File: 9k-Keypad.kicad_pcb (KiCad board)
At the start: 2 copper layers, 66.7 x 4 mm, 36 parts, among them J1 USB_C_Receptacle_USB2.0, U1 ATmega32U4-AU, Y1 16MHz

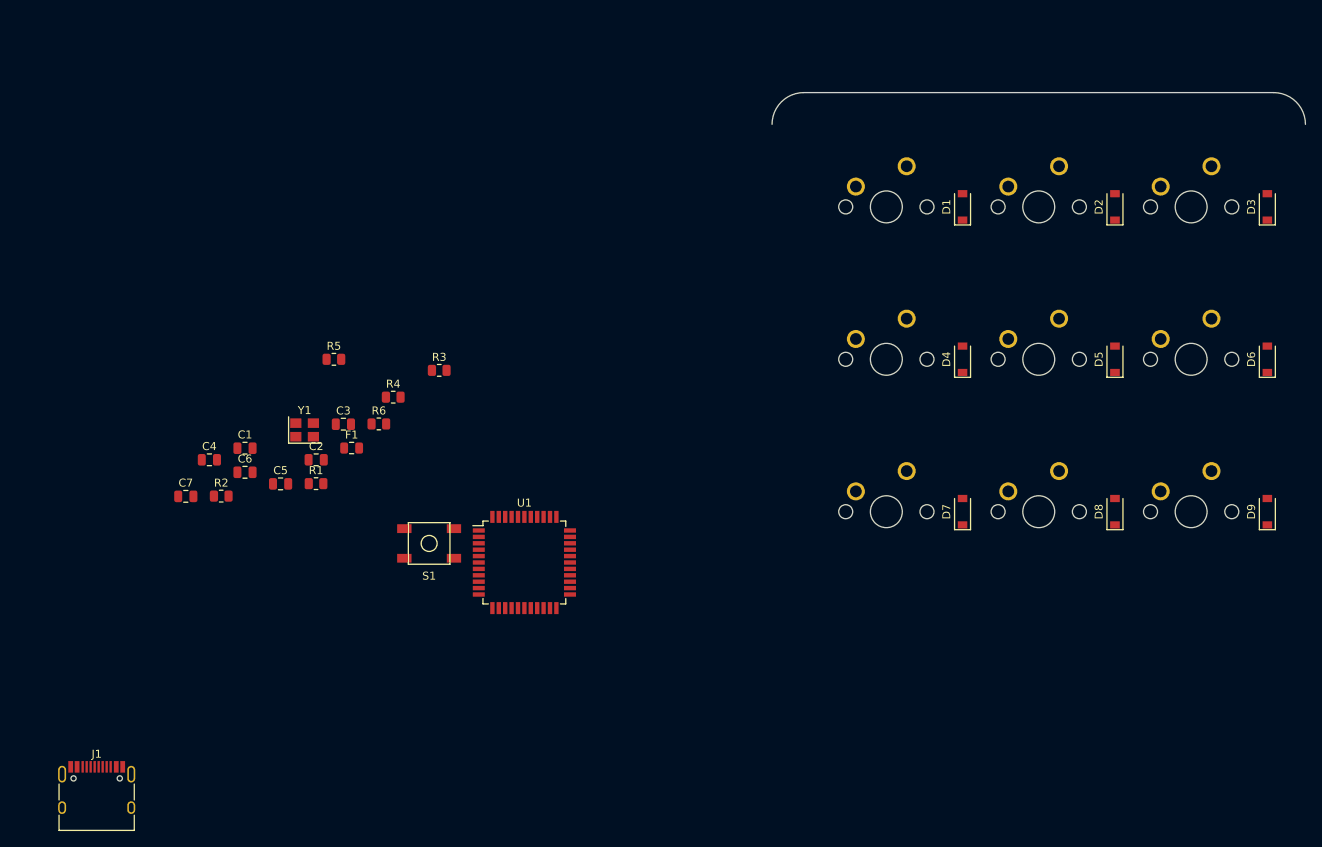
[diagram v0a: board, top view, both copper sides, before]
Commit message: fix various routing issues
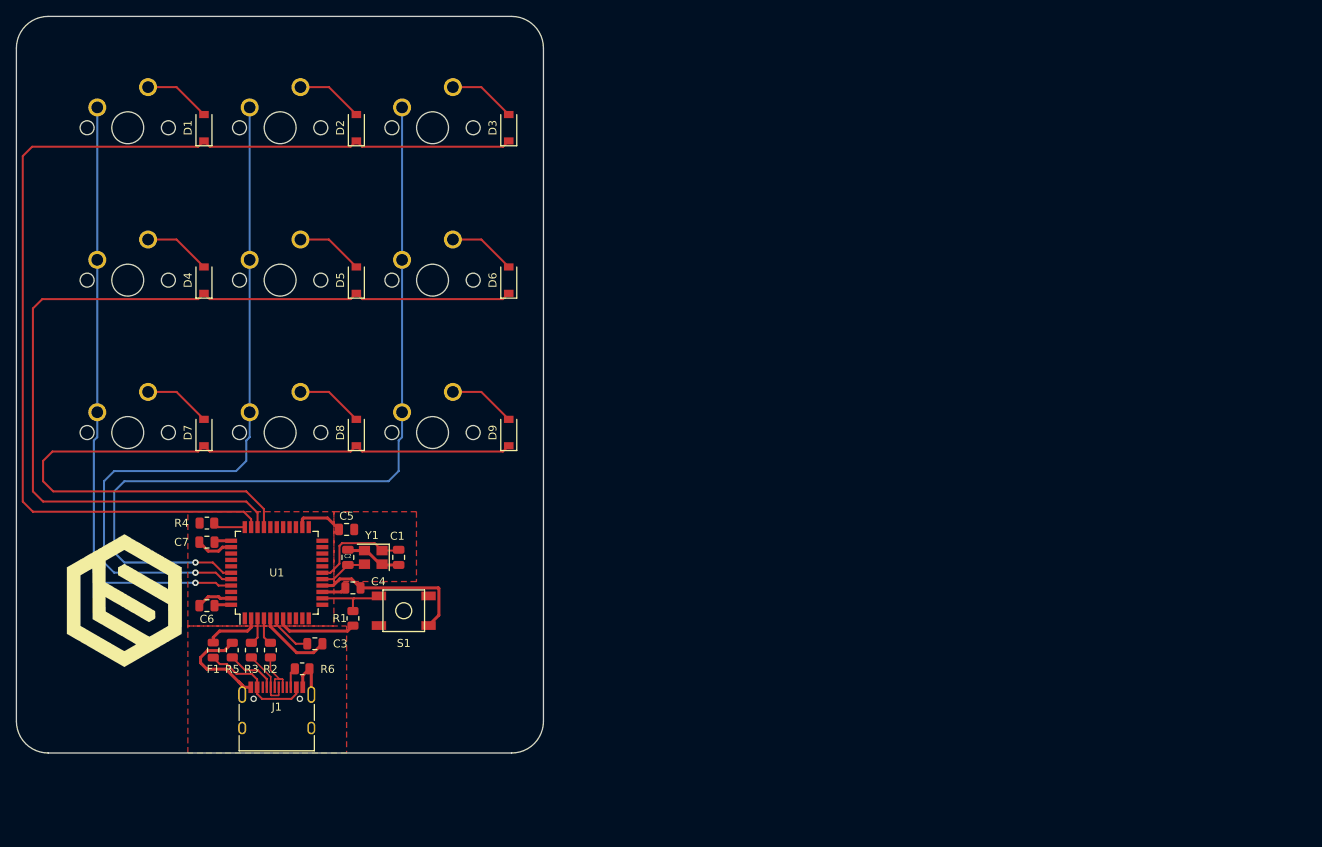
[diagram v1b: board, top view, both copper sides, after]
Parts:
- added G***: LOGO, kiCad 6.0:SL Logo, F.Cu at (95.2, 138.1)
- moved D1 95.3 mm to (105.2, 79.0)
- moved D4 95.3 mm to (105.2, 98.1)
- moved D7 95.3 mm to (105.2, 117.1)
- moved MX1 95.3 mm to (95.7, 79.0)
- moved MX2 95.3 mm to (114.7, 79.0)
- moved MX4 95.3 mm to (95.7, 98.1)
- moved MX5 95.3 mm to (114.7, 98.1)
- moved MX7 95.3 mm to (95.7, 117.1)
- moved MX8 95.3 mm to (114.7, 117.1)
- moved D2 95.3 mm to (124.3, 79.0)
- moved D3 95.3 mm to (143.3, 79.0)
- moved D5 95.3 mm to (124.3, 98.1)
- moved D6 95.3 mm to (143.3, 98.1)
- moved D8 95.3 mm to (124.3, 117.1)
- moved D9 95.3 mm to (143.3, 117.1)
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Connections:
- U1 pad 30: unconnected-(U1-Pad30) -> ROW2
- U1 pad 31: unconnected-(U1-Pad31) -> ROW1
- U1 pad 32: unconnected-(U1-Pad32) -> ROW0
- U1 pad 39: unconnected-(U1-Pad39) -> COL2
- U1 pad 40: unconnected-(U1-Pad40) -> COL1
- U1 pad 41: unconnected-(U1-Pad41) -> COL0
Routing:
- net ROW0: track 0.00 -> 136.4 mm
- net ROW1: track 0.00 -> 115.3 mm
- net COL2: track 0.00 -> 105.5 mm, vias 0 -> 1
- net ROW2: track 0.00 -> 94.0 mm
- net COL1: track 0.00 -> 90.1 mm, vias 0 -> 1
- net COL0: track 0.00 -> 76.2 mm, vias 0 -> 1
- net GND: track 0.00 -> 66.9 mm
- net +5V: track 0.00 -> 30.8 mm
- net VCC: track 0.00 -> 14.7 mm
- net Net-(C1-Pad1): track 0.00 -> 12.8 mm
- net Net-(R1-Pad2): track 0.00 -> 8.84 mm
- net Net-(D3-Pad2): track 0.00 -> 8.41 mm
- net Net-(D9-Pad2): track 0.00 -> 8.41 mm
- net Net-(D6-Pad2): track 0.00 -> 8.41 mm
- net Net-(D2-Pad2): track 0.00 -> 8.41 mm
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- added copper zone on F.Cu, net GND
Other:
- board size 66.7 x 4 mm -> 65.9 x 92.1 mm

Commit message: Finished Design
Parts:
- added REF**: MountingHole_3.5mm, MountingHole:MountingHole_3.5mm, F.Cu at (85.7, 69.1)
- added REF**: MountingHole_3.5mm, MountingHole:MountingHole_3.5mm, F.Cu at (143.7, 151.6)
- added REF**: MountingHole_3.5mm, MountingHole:MountingHole_3.5mm, F.Cu at (143.7, 69.1)
- added REF**: MountingHole_3.5mm, MountingHole:MountingHole_3.5mm, F.Cu at (85.7, 151.6)
- moved C4 8.09 mm to (131.8, 134.9), turned to 90 degrees
- moved C7 3.18 mm to (102.4, 131.0), turned to -90 degrees
- moved C5 0.63 mm to (123.0, 128.6)
- moved R4 0.16 mm to (105.6, 128.6)
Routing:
- net +5V: track 30.8 -> 128.1 mm, vias 0 -> 3
- net GND: track 66.9 -> 95.5 mm, vias 0 -> 5
- net Net-(R4-Pad2): track 4.03 -> 3.48 mm
- added copper zone on B.Cu, net GND
- removed copper zone on F.Cu, net GND
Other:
- board size 65.9 x 92.1 mm -> 65.9 x 90.5 mm
